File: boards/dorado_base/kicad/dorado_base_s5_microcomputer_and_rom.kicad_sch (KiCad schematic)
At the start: 4 parts

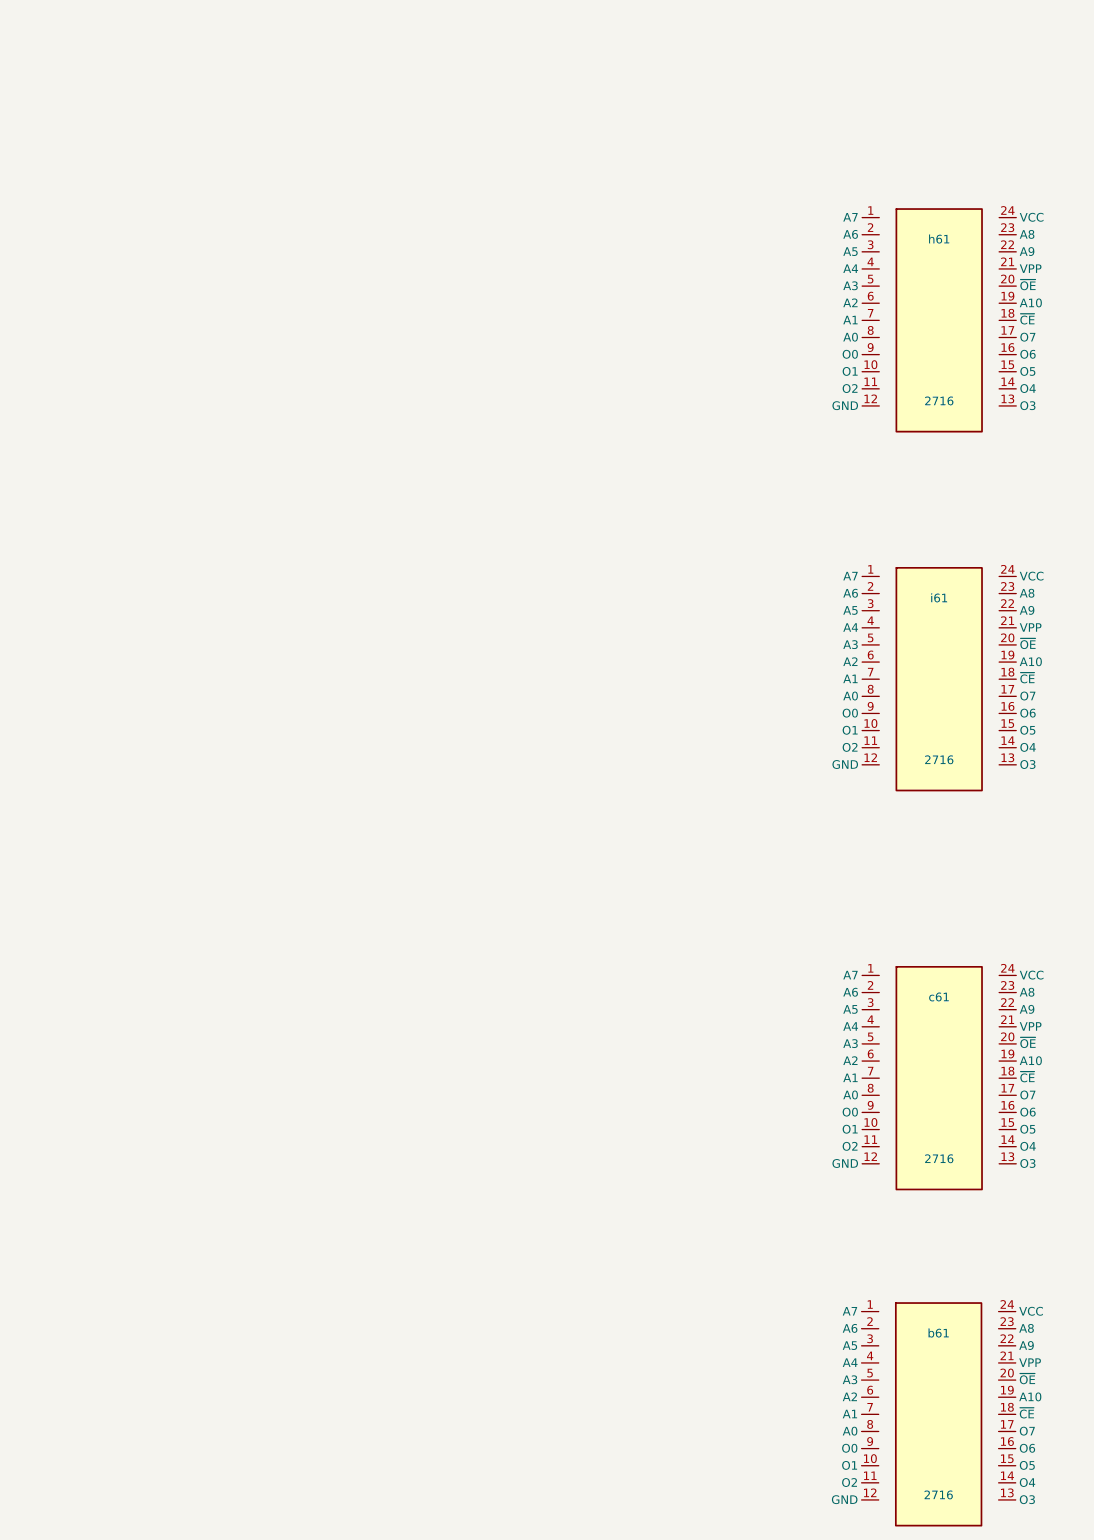
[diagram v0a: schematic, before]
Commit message: Dorado p5: vision-placed bboxes, named bus nets, tracer dot-kernel fix
Vision-driven recognition (per the deterministic-vs-LLM split now codified
in AGENTS.md): bboxes for e07/g08/c08/f61/g11 placed by reading page-5
tiles directly rather than running snap-board, after cartographer's CV
snap kept picking sub-rectangles inside the chip body. h61's pin
positions are translated to the other 3 EPROMs by bbox-delta — same chip
drawn identically, so the translation is purely geometric.

Added 19 named-label nets covering the address bus (MCA.00..10) and
data bus (MCD.0..7) joining the 6502 to all 4 on-page EPROMs. Single-
endpoint cross-sheet labels (MCNMI', RomN', etc.) are noted in the
session but not yet in graph.json — validator requires 2+ endpoints
and we haven't relaxed that rule for label-typed nets.

Tracer: dot-detection kernel default 3→7 (ELLIPSE) so wire strokes
finally get erased on 300 DPI scans; before, the dots layer covered
~97% of foreground and every junction passed the dot test. The
junction-detect path itself still over-breaks because the line layer
isn't 1-px-thin (no skimage / opencv-contrib available); it's now
documented as needing proper Zhang-Suen thinning. With junction-detect
off, the tracer assigns 90/96 EPROM pins on Dorado p5.

Librarian: + 74LS163, + MCS6502 (now 17 chips).
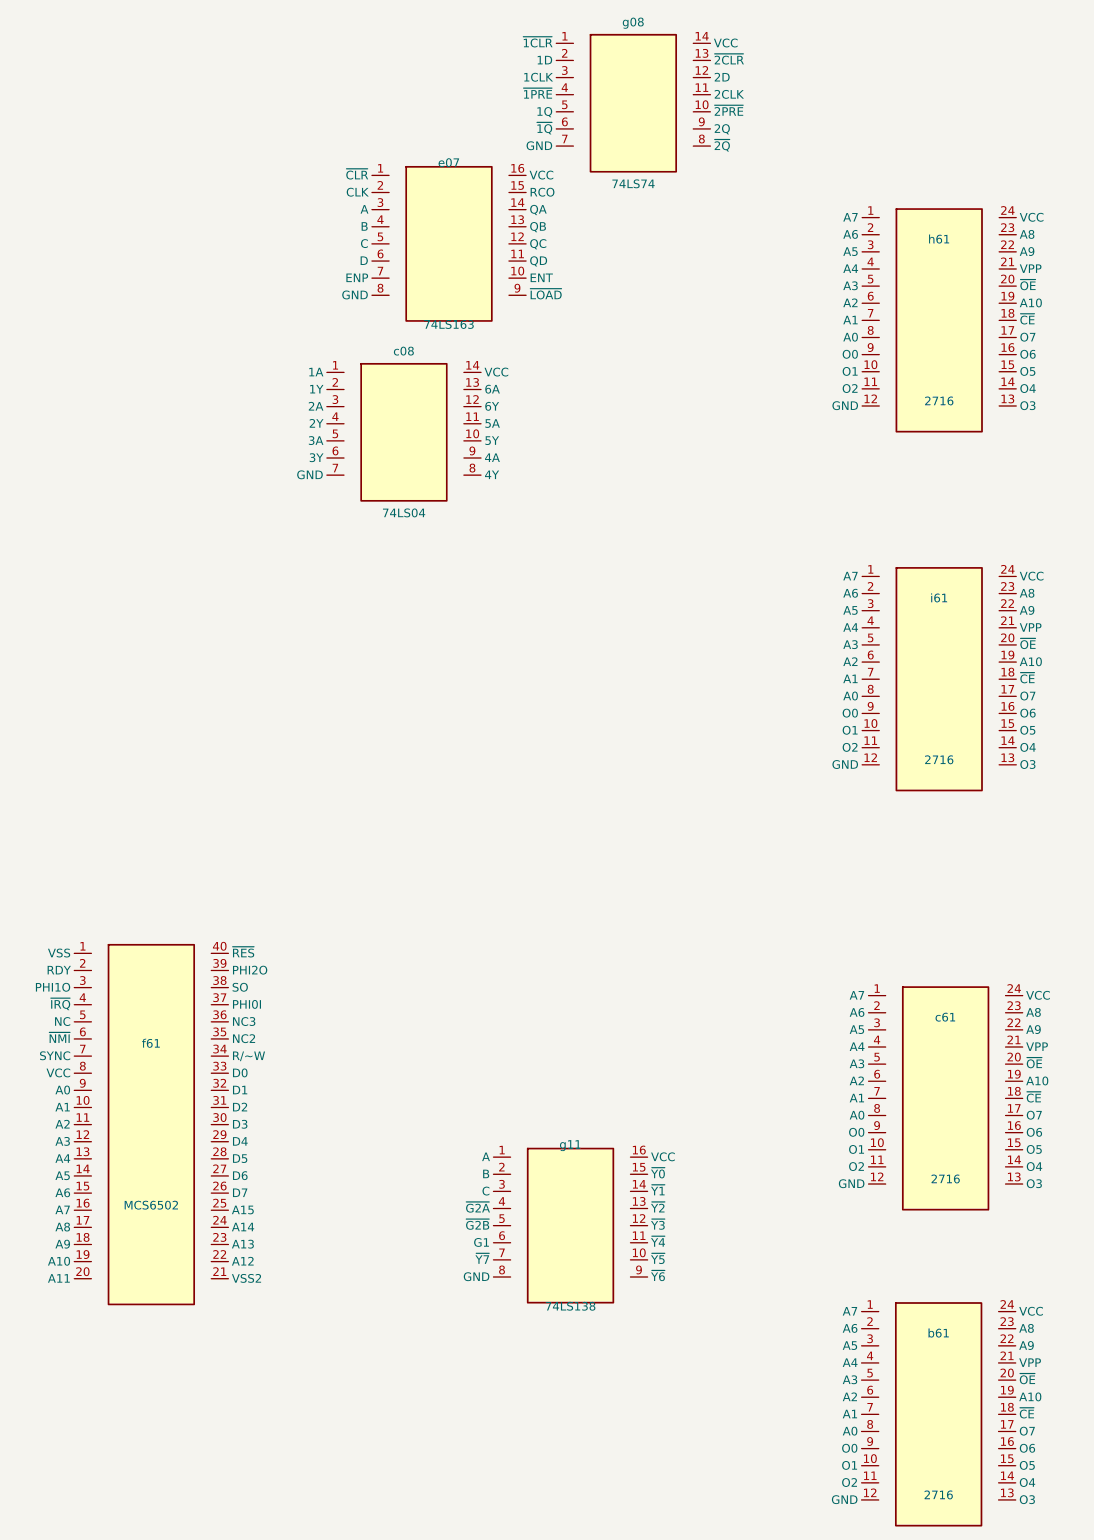
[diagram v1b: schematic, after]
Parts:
- added c08: 74LS04, symbol user:74LS04
- added e07: 74LS163, symbol user:74LS163
- added f61: MCS6502, symbol user:MCS6502
- added g08: 74LS74, symbol user:74LS74
- added g11: 74LS138, symbol user:74LS138
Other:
- moved on the sheet: c61
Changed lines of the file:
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@@
   (symbol
     (lib_id "user:2716")
-    (at 186.938 187.14 0)
-    (unit 1)
-    (exclude_from_sim no)
-    (in_bom yes)
-    (on_board yes)
-    (dnp no)
-    (property "Reference" "c61" (at 186.938 175.14 0)
-      (effects (font (size 1.27 1.27))))
-    (property "Value" "2716" (at 186.938 199.14 0)
-      (effects (font (size 1.27 1.27))))
-    (property "Footprint" "" (at 186.938 187.14 0)
-      (effects (font (size 1.27 1.27)) (hide yes)))
-    (property "Datasheet" "" (at 186.938 187.14 0)
+    (at 187.89 190.138 0)
+    (unit 1)
+    (exclude_from_sim no)
+    (in_bom yes)
+    (on_board yes)
+    (dnp no)
+    (property "Reference" "c61" (at 187.89 178.138 0)
+      (effects (font (size 1.27 1.27))))
+    (property "Value" "2716" (at 187.89 202.138 0)
+      (effects (font (size 1.27 1.27))))
+    (property "Footprint" "" (at 187.89 190.138 0)
+      (effects (font (size 1.27 1.27)) (hide yes)))
+    (property "Datasheet" "" (at 187.89 190.138 0)
       (effects (font (size 1.27 1.27)) (hide yes)))
     (pin "1")
@@
         )
       )
+    )
+  )
+  (symbol
+    (lib_id "user:74LS74")
+    (at 141.574 42.5425 0)
+    (unit 1)
+    (exclude_from_sim no)
+    (in_bom yes)
+    (on_board yes)
+    (dnp no)
+    (property "Reference" "g08" (at 141.574 30.5425 0)
+      (effects (font (size 1.27 1.27))))
+    (property "Value" "74LS74" (at 141.574 54.5425 0)
+      (effects (font (size 1.27 1.27))))
+    (property "Footprint" "" (at 141.574 42.5425 0)
+      (effects (font (size 1.27 1.27)) (hide yes)))
+    (property "Datasheet" "" (at 141.574 42.5425 0)
+      (effects (font (size 1.27 1.27)) (hide yes)))
+    (pin "1")
+    (pin "2")
+    (pin "3")
+    (pin "4")
+    (pin "5")
+    (pin "6")
+    (pin "7")
+    (pin "8")
+    (pin "9")
+    (pin "10")
+    (pin "11")
+    (pin "12")
+    (pin "13")
+    (pin "14")
+    (instances
+      (project "dorado_base"
+        (path "/03250789-4823-e1d8-1826-a7dc8de71907"
+          (reference "g08") (unit 1)
+        )
+      )
+    )
+  )
+  (symbol
+    (lib_id "user:74LS04")
+    (at 107.551 91.3494 0)
+    (unit 1)
+    (exclude_from_sim no)
+    (in_bom yes)
+    (on_board yes)
+    (dnp no)
+    (property "Reference" "c08" (at 107.551 79.3494 0)
+      (effects (font (size 1.27 1.27))))
+    (property "Value" "74LS04" (at 107.551 103.349 0)
+      (effects (font (size 1.27 1.27))))
+    (property "Footprint" "" (at 107.551 91.3494 0)
+      (effects (font (size 1.27 1.27)) (hide yes)))
+    (property "Datasheet" "" (at 107.551 91.3494 0)
+      (effects (font (size 1.27 1.27)) (hide yes)))
+    (pin "1")
+    (pin "2")
+    (pin "3")
+    (pin "4")
+    (pin "5")
+    (pin "6")
+    (pin "7")
+    (pin "8")
+    (pin "9")
+    (pin "10")
+    (pin "11")
+    (pin "12")
+    (pin "13")
+    (pin "14")
+    (instances
+      (project "dorado_base"
+        (path "/03250789-4823-e1d8-1826-a7dc8de71907"
+          (reference "c08") (unit 1)
+        )
+      )
+    )
+  )
+  (symbol
+    (lib_id "user:74LS163")
+    (at 114.234 63.4019 0)
+    (unit 1)
+    (exclude_from_sim no)
+    (in_bom yes)
+    (on_board yes)
+    (dnp no)
+    (property "Reference" "e07" (at 114.234 51.4019 0)
+      (effects (font (size 1.27 1.27))))
+    (property "Value" "74LS163" (at 114.234 75.4019 0)
+      (effects (font (size 1.27 1.27))))
+    (property "Footprint" "" (at 114.234 63.4019 0)
+      (effects (font (size 1.27 1.27)) (hide yes)))
+    (property "Datasheet" "" (at 114.234 63.4019 0)
+      (effects (font (size 1.27 1.27)) (hide yes)))
+    (pin "1")
+    (pin "2")
+    (pin "3")
+    (pin "4")
+    (pin "5")
+    (pin "6")
+    (pin "7")
+    (pin "8")
+    (pin "9")
+    (pin "10")
+    (pin "11")
+    (pin "12")
+    (pin "13")
+    (pin "14")
+    (pin "15")
+    (pin "16")
+    (instances
+      (project "dorado_base"
+        (path "/03250789-4823-e1d8-1826-a7dc8de71907"
+          (reference "e07") (unit 1)
+        )
+      )
+    )
+  )
+  (symbol
+    (lib_id "user:MCS6502")
+    (at 70.085 194.026 0)
+    (unit 1)
+    (exclude_from_sim no)
+    (in_bom yes)
+    (on_board yes)
+    (dnp no)
+    (property "Reference" "f61" (at 70.085 182.026 0)
+      (effects (font (size 1.27 1.27))))
+    (property "Value" "MCS6502" (at 70.085 206.026 0)
+      (effects (font (size 1.27 1.27))))
+    (property "Footprint" "" (at 70.085 194.026 0)
+      (effects (font (size 1.27 1.27)) (hide yes)))
+    (property "Datasheet" "" (at 70.085 194.026 0)
+      (effects (font (size 1.27 1.27)) (hide yes)))
+    (pin "1")
+    (pin "2")
+    (pin "3")
+    (pin "4")
+    (pin "5")
+    (pin "6")
+    (pin "7")
+    (pin "8")
+    (pin "9")
+    (pin "10")
+    (pin "11")
+    (pin "12")
+    (pin "13")
+    (pin "14")
+    (pin "15")
+    (pin "16")
+    (pin "17")
+    (pin "18")
+    (pin "19")
+    (pin "20")
+    (pin "21")
+    (pin "22")
+    (pin "23")
+    (pin "24")
+    (pin "25")
+    (pin "26")
+    (pin "27")
+    (pin "28")
+    (pin "29")
+    (pin "30")
+    (pin "31")
+    (pin "32")
+    (pin "33")
+    (pin "34")
+    (pin "35")
+    (pin "36")
+    (pin "37")
+    (pin "38")
+    (pin "39")
+    (pin "40")
+    (instances
+      (project "dorado_base"
+        (path "/03250789-4823-e1d8-1826-a7dc8de71907"
+          (reference "f61") (unit 1)
+        )
+      )
+    )
+  )
+  (symbol
+    (lib_id "user:74LS138")
+    (at 132.258 209.012 0)
+    (unit 1)
+    (exclude_from_sim no)
+    (in_bom yes)
+    (on_board yes)
+    (dnp no)
+    (property "Reference" "g11" (at 132.258 197.012 0)
+      (effects (font (size 1.27 1.27))))
+    (property "Value" "74LS138" (at 132.258 221.012 0)
+      (effects (font (size 1.27 1.27))))
+    (property "Footprint" "" (at 132.258 209.012 0)
+      (effects (font (size 1.27 1.27)) (hide yes)))
+    (property "Datasheet" "" (at 132.258 209.012 0)
+      (effects (font (size 1.27 1.27)) (hide yes)))
+    (pin "1")
+    (pin "2")
+    (pin "3")
+    (pin "4")
+    (pin "5")
+    (pin "6")
+    (pin "7")
+    (pin "8")
+    (pin "9")
+    (pin "10")
+    (pin "11")
+    (pin "12")
+    (pin "13")
+    (pin "14")
+    (pin "15")
+    (pin "16")
+    (instances
+      (project "dorado_base"
+        (path "/03250789-4823-e1d8-1826-a7dc8de71907"
+          (reference "g11") (unit 1)
+        )
+      )

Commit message: Sheet-5 cleanup: missing components, KiCad label emit, validator relax
Components: + d08 (MC12061 oscillator) and + c07 (JUMPER_PLUG_16
EPROM-jumpers socket) — both visible on page 5 but previously dropped
because there was no librarian entry. Added MC12061 (pinout transcribed
from the schematic itself; needs datasheet verification) and a generic
JUMPER_PLUG_16 stub for the routing socket. Page-5 graph now has 11
components covering every drawn chip.

KiCad export: emit (label ...) for edge_type=label nets and
(global_label ...) for sheet_zone / off_page nets — previously these
were silently dropped, leaving the exported schematic wireless. Sanitise
KiCad-hostile characters in net names ("'" → "~{...}" overbar, "/" →
"_") since KiCad refuses to load schematics with those literals in label
names. Plain (label ...) entities can't carry (shape ...), only
(global_label ...) and (hierarchical_label ...) — restrict accordingly.

Validator relax: allow single-endpoint nets with edge_type label /
sheet_zone / off_page (signals that legitimately have one endpoint per
sheet because the rest of the net lives on other sheets that haven't
been transcribed yet). edge_type=wire / bus / implicit_power still
require ≥2 endpoints.

Added 23 cross-sheet labelled signals (MCNMI', MCIRQ', MCReset',
MCR/W', MCClk/MCClk'/MCPreClk, RSA.0..2, Rom0'..Rom7', MCA.11..15) — 42
nets total on sheet 5.
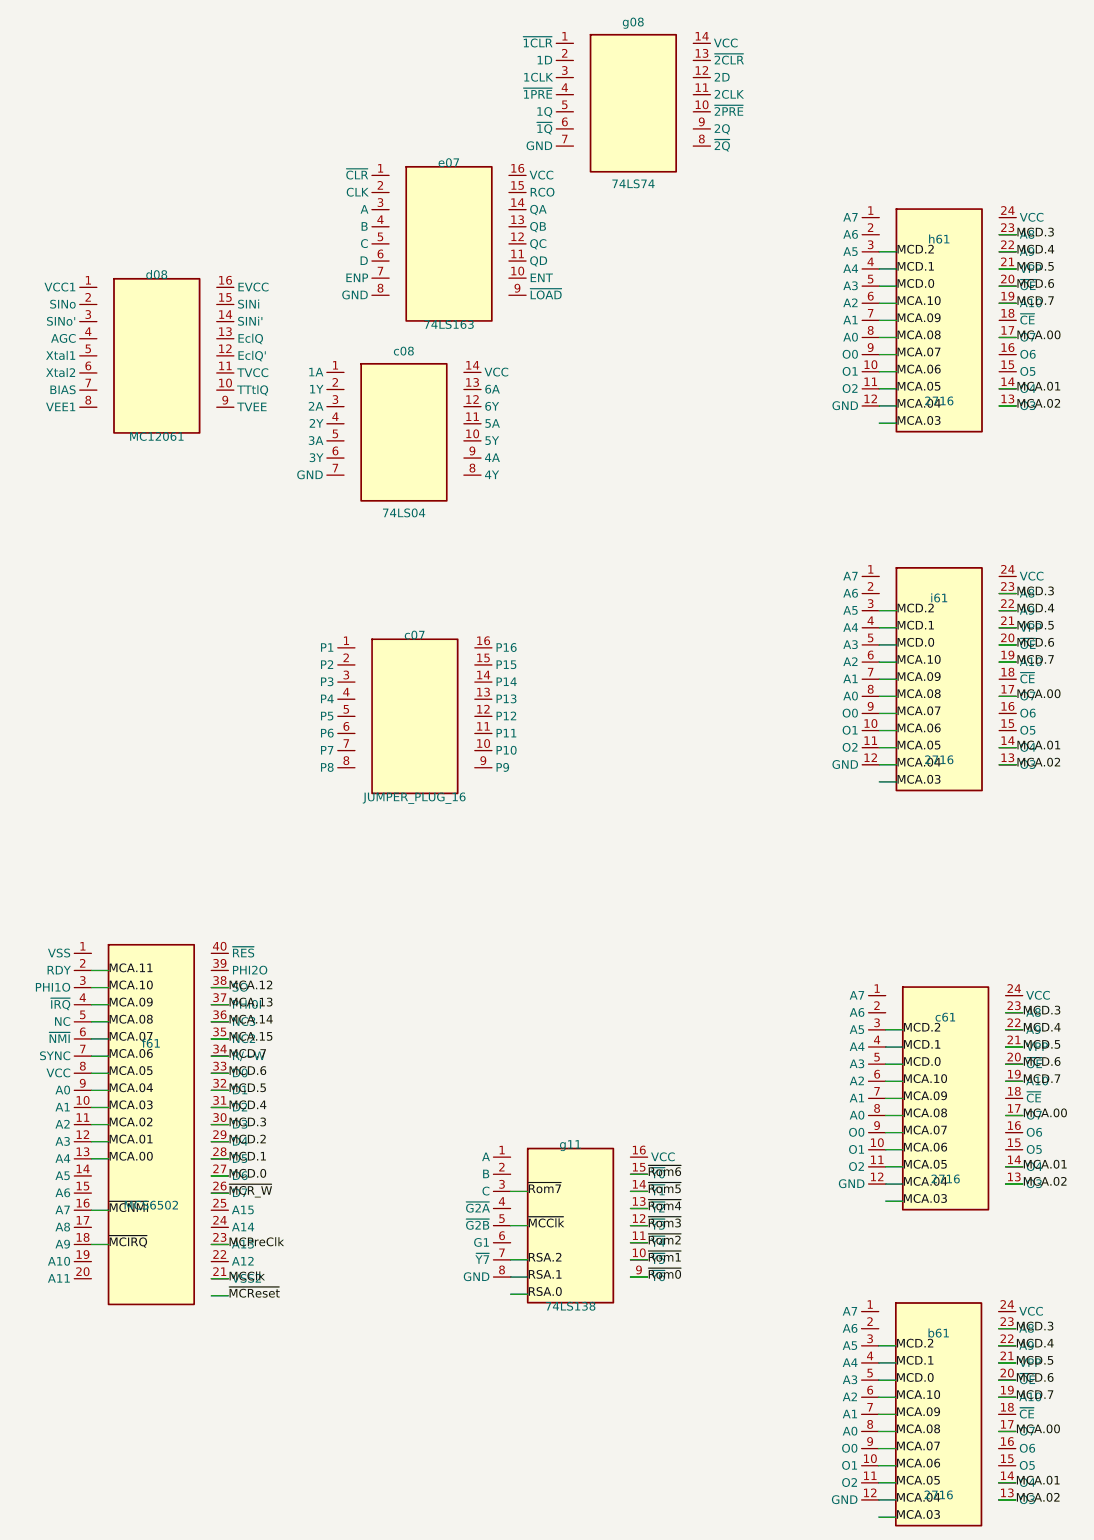
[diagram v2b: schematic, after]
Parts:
- added c07: JUMPER_PLUG_16, symbol user:JUMPER_PLUG_16
- added d08: MC12061, symbol user:MC12061
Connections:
- net MCA.06: now reaches h61.10 (O1)
- net MCA.06: now also b61.10 (O1), c61.10 (O1), f61.7 (SYNC), i61.10 (O1)
- net MCA.05: now reaches h61.11 (O2)
- net MCA.05: now also b61.11 (O2), c61.11 (O2), f61.8 (VCC), i61.11 (O2)
- net MCA.04: now reaches h61.12 (GND)
- net MCA.04: now also b61.12 (GND), c61.12 (GND), f61.9 (A0), i61.12 (GND)
- net MCA.02: now reaches h61.13 (O3)
- net MCA.02: now also b61.13 (O3), c61.13 (O3), f61.11 (A2), i61.13 (O3)
- net MCA.01: now reaches h61.14 (O4)
- net MCA.01: now also b61.14 (O4), c61.14 (O4), f61.12 (A3), i61.14 (O4)
- net MCA.00: now reaches h61.17 (O7)
- net MCA.00: now also b61.17 (O7), c61.17 (O7), f61.13 (A4), i61.17 (O7)
- net MCD.7: now reaches h61.19 (A10)
- net MCD.7: now also b61.19 (A10), c61.19 (A10), f61.34 (R/~W), i61.19 (A10)
- net MCD.6: now reaches h61.20 (~{OE})
- net MCD.6: now also b61.20 (~{OE}), c61.20 (~{OE}), f61.33 (D0), i61.20 (~{OE})
- net MCD.5: now reaches h61.21 (VPP)
- net MCD.5: now also b61.21 (VPP), c61.21 (VPP), f61.32 (D1), i61.21 (VPP)
- net MCD.4: now reaches h61.22 (A9)
- net MCD.4: now also b61.22 (A9), c61.22 (A9), f61.31 (D2), i61.22 (A9)
- net MCD.3: now reaches h61.23 (A8)
- net MCD.3: now also b61.23 (A8), c61.23 (A8), f61.30 (D3), i61.23 (A8)
- net MCD.2: now reaches h61.3 (A5)
- net MCD.2: now also b61.3 (A5), c61.3 (A5), f61.29 (D4), i61.3 (A5)
- net MCD.1: now reaches h61.4 (A4)
- net MCD.1: now also b61.4 (A4), c61.4 (A4), f61.28 (D5), i61.4 (A4)
- net MCD.0: now reaches h61.5 (A3)
- net MCD.0: now also b61.5 (A3), c61.5 (A3), f61.27 (D6), i61.5 (A3)
- net MCA.10: now reaches h61.6 (A2)
- net MCA.10: now also b61.6 (A2), c61.6 (A2), f61.3 (PHI1O), i61.6 (A2)
- net MCA.09: now reaches h61.7 (A1)
- net MCA.09: now also b61.7 (A1), c61.7 (A1), f61.4 (~{IRQ}), i61.7 (A1)
- net MCA.08: now reaches h61.8 (A0)
- net MCA.08: now also b61.8 (A0), c61.8 (A0), f61.5 (NC), i61.8 (A0)
- net MCA.07: now reaches h61.9 (O0)
- net MCA.07: now also b61.9 (O0), c61.9 (O0), f61.6 (~{NMI}), i61.9 (O0)
- net MCA.03: now reaches f61.10 (A1)
- net ~{MCNMI}: now reaches f61.16 (A7)
- net ~{MCIRQ}: now reaches f61.18 (A9)
- net MCA.11: now reaches f61.2 (RDY)
- net MCClk: now reaches f61.21 (VSS2)
- net MCPreClk: now reaches f61.23 (A13)
- net ~{MCR_W}: now reaches f61.26 (D7)
- net MCA.15: now reaches f61.35 (NC2)
- net MCA.14: now reaches f61.36 (NC3)
- net MCA.13: now reaches f61.37 (PHI0I)
- net MCA.12: now reaches f61.38 (SO)
- net ~{Rom1}: now reaches g11.10 (~{Y5})
- net ~{Rom2}: now reaches g11.11 (~{Y4})
- net ~{Rom3}: now reaches g11.12 (~{Y3})
- net ~{Rom4}: now reaches g11.13 (~{Y2})
- net ~{Rom5}: now reaches g11.14 (~{Y1})
- net ~{Rom6}: now reaches g11.15 (~{Y0})
- net ~{Rom7}: now reaches g11.3 (C)
- net ~{MCClk}: now reaches g11.5 (~{G2B})
- net RSA.2: now reaches g11.7 (~{Y7})
- net RSA.1: now reaches g11.8 (GND)
- net ~{Rom0}: now reaches g11.9 (~{Y6})
